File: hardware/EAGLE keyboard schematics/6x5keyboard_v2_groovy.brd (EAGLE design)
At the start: 117.8 x 116.8 mm, 71 parts

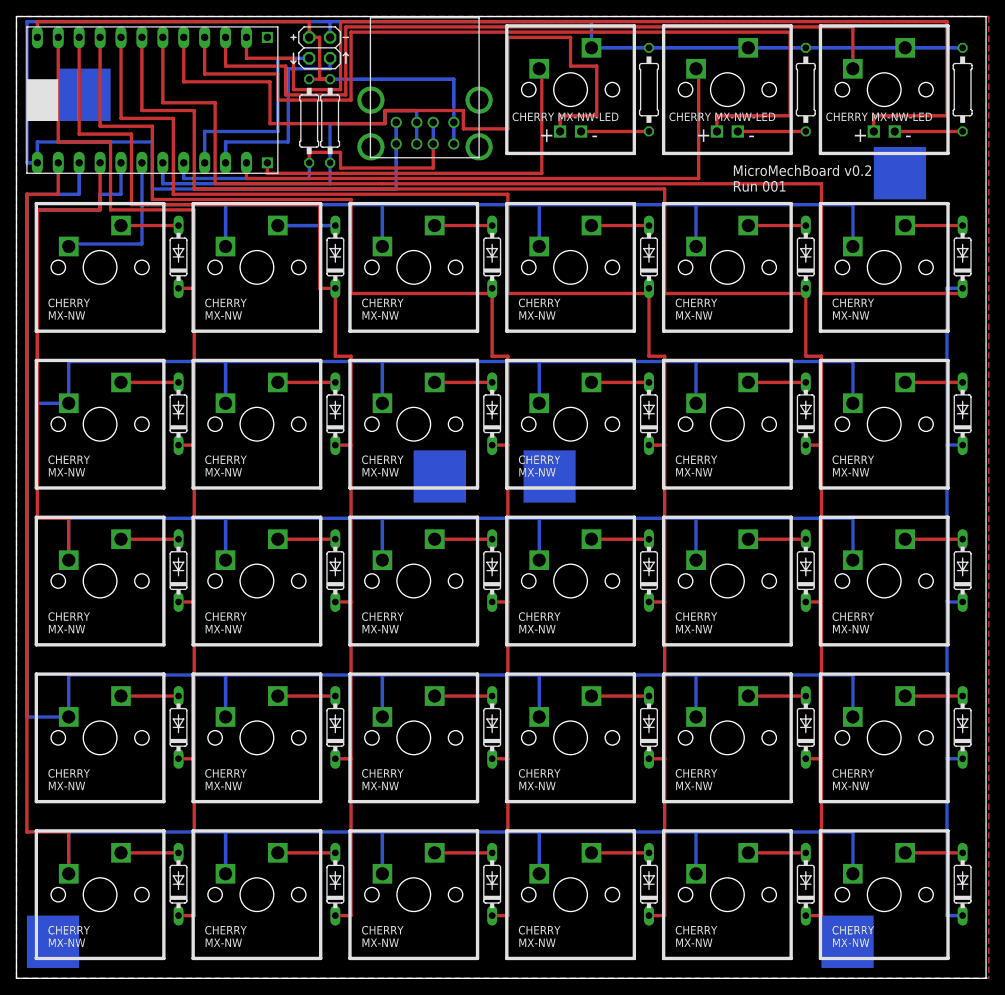
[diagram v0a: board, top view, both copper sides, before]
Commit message: Groovy traces now in their own files.  6x5keyboard_v2_untested.* is exclusively right-angle traces now.
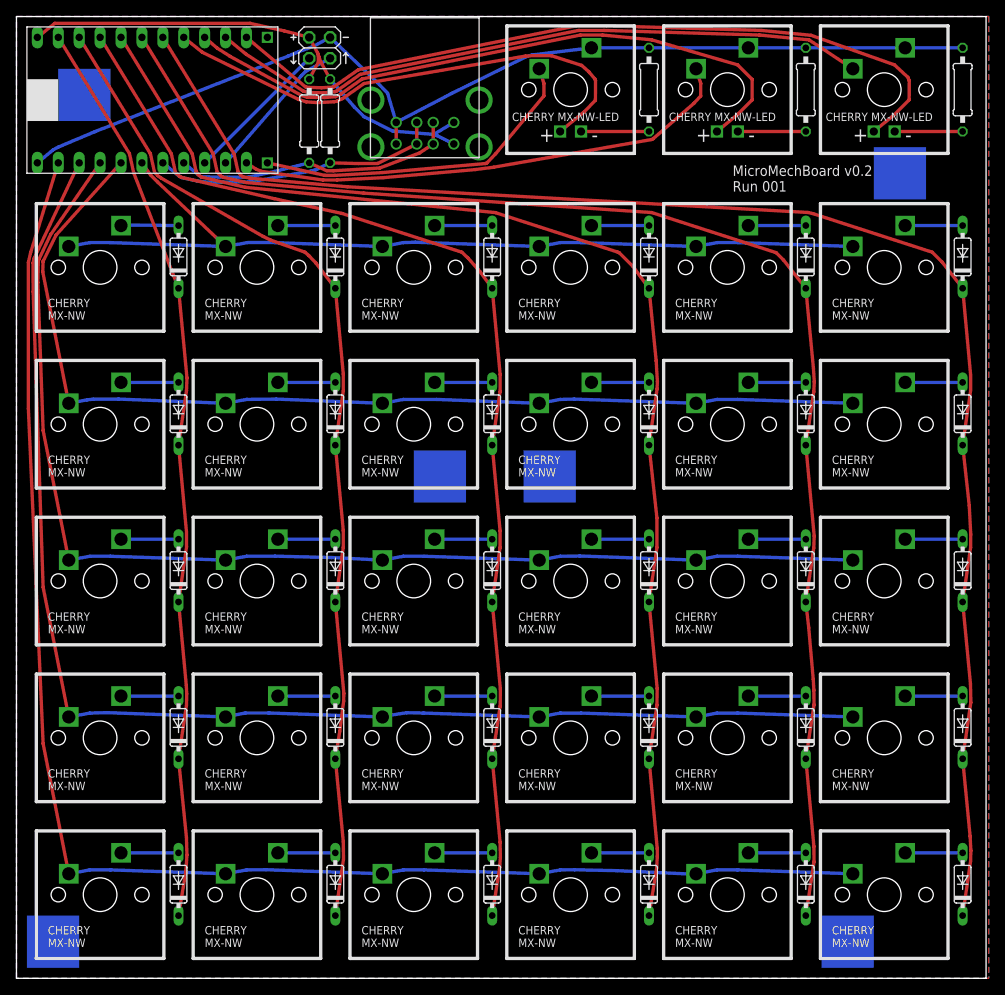
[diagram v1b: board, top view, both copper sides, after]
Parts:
- added U$36, U$37, U$38, U$39, U$40, U$41: MOUNTING-PAD, my_parts:MOUNTING-PAD
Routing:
- net GND: track 197.1 -> 125.7 mm
- net N$39: track 168.9 -> 128.4 mm
- net N$37: track 204.5 -> 164.4 mm
- net N$38: track 185.4 -> 146.3 mm
- net N$41: track 221.0 -> 182.8 mm
- net N$47: track 91.8 -> 62.1 mm
- net N$46: track 108.0 -> 79.2 mm
- net N$54: track 121.9 -> 93.5 mm
- net N$36: track 214.6 -> 186.7 mm
- net N$35: track 198.1 -> 170.3 mm
- net N$34: track 181.6 -> 153.9 mm
- net N$33: track 165.1 -> 137.5 mm
- net N$32: track 147.3 -> 122.1 mm
- net N$31: track 132.7 -> 110.7 mm
- net N$40: track 130.8 -> 109.9 mm
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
